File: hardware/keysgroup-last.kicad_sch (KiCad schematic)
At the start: 19 parts, among them SW65 SC4823S6-TR, SW66 SC4823S6-TR, SW67 SC4823S6-TR, SW68 SC4823S6-TR, SW69 SC4823S6-TR, SW70 SC4823S6-TR, SW71 SC4823S6-TR, SW72 SC4823S6-TR, SW73 SC4823S6-TR, SW74 SC4823S6-TR, SW75 SC4823S6-TR, SW76 SC4823S6-TR, SW77 SC4823S6-TR, SW78 SC4823S6-TR, T5 XL4067TS

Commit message: :construction: some chip layout
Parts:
- C29: symbol components:0402,100nF -> KeysDock:0402,100nF
- C30: symbol components:0402,4.7uF -> KeysDock:0402,4.7uF
- C31: symbol components:0402,10uF -> KeysDock:0402,10uF
- T5: symbol components:XL4067TS -> KeysDock:XL4067TS
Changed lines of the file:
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@@
 	)
 	(symbol
-		(lib_id "components:0402,10uF")
+		(lib_id "KeysDock:0402,10uF")
 		(at 247.65 129.54 0)
 		(unit 1)
@@
 	)
 	(symbol
-		(lib_id "components:0402,100nF")
+		(lib_id "KeysDock:0402,100nF")
 		(at 237.49 129.54 0)
 		(unit 1)
@@
 	)
 	(symbol
-		(lib_id "components:0402,4.7uF")
+		(lib_id "KeysDock:0402,4.7uF")
 		(at 242.57 129.54 0)
 		(unit 1)
@@
 	)
 	(symbol
-		(lib_id "components:XL4067TS")
+		(lib_id "KeysDock:XL4067TS")
 		(at 217.17 113.03 270)
 		(unit 1)

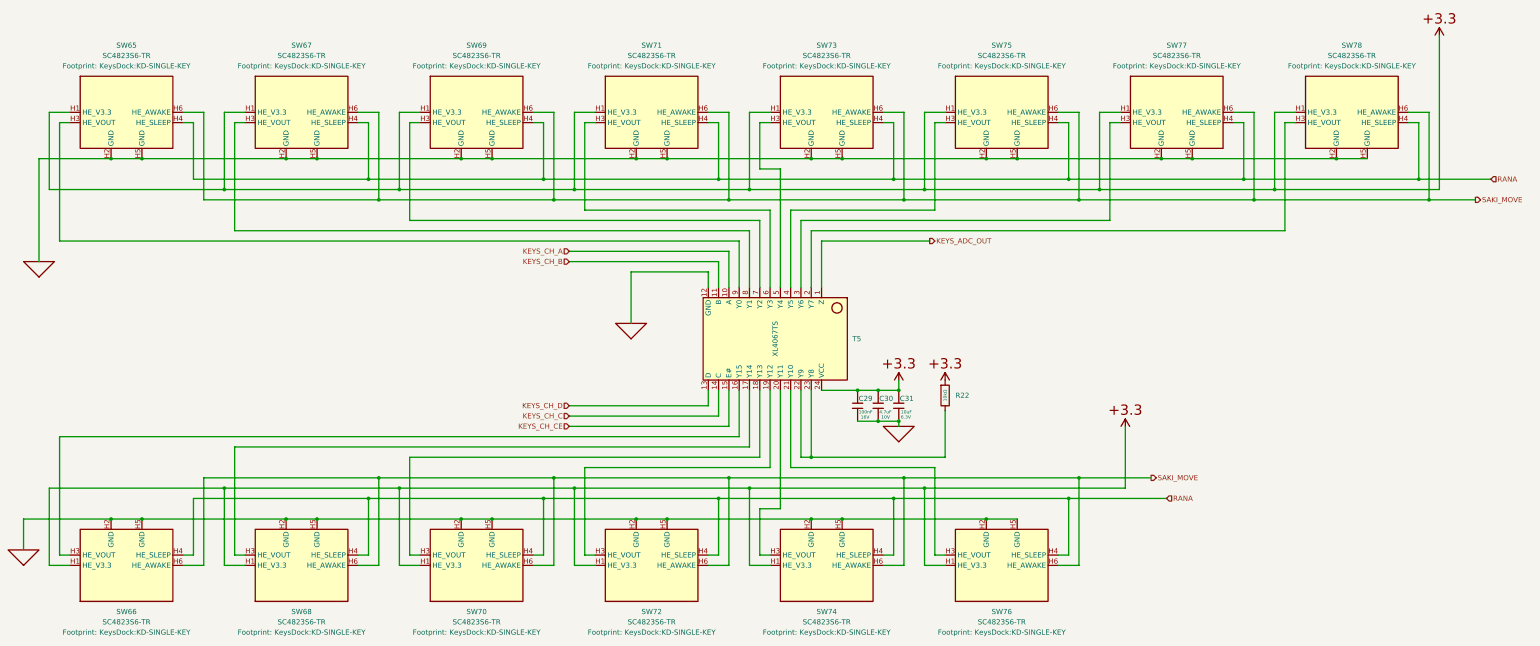
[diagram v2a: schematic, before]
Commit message: :sparkles: use net tie to construct GNDs
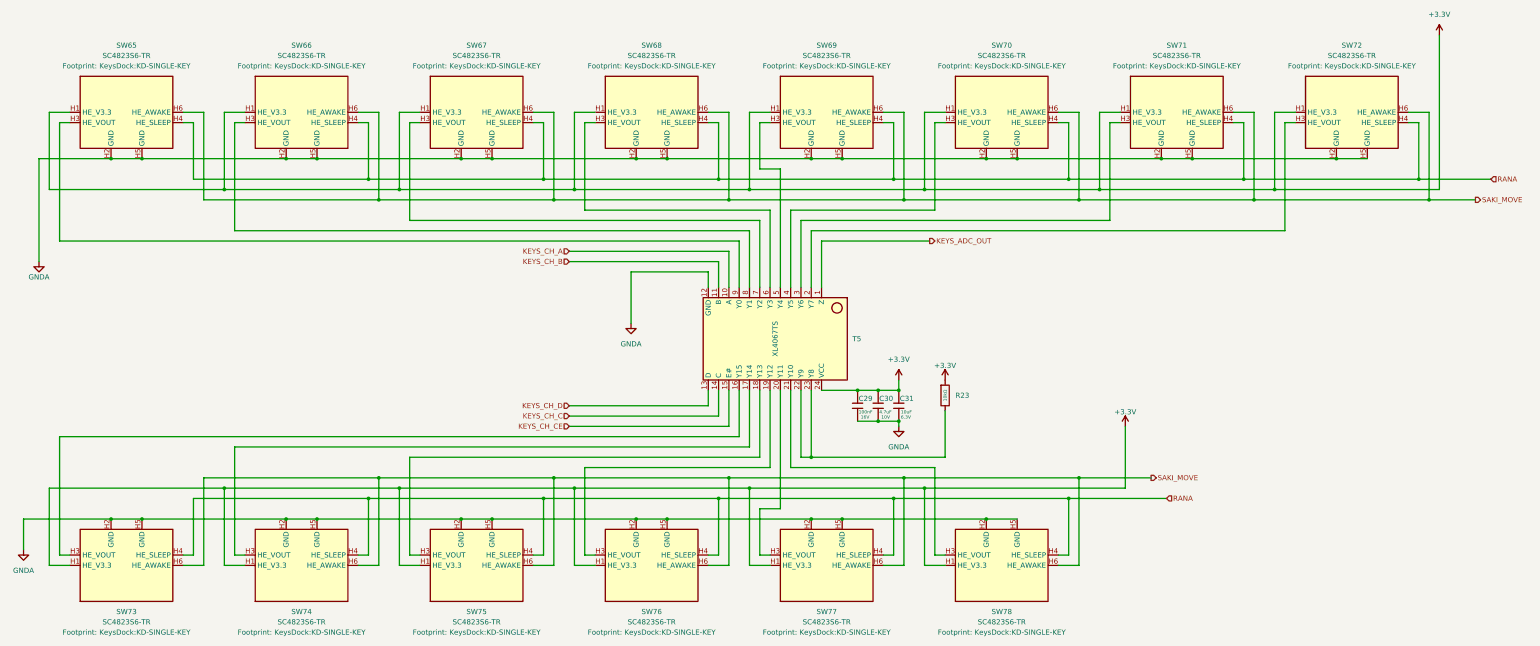
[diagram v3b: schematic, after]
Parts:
- renumbered R22 to R23, SW67 to SW66, SW69 to SW67, SW71 to SW68, SW73 to SW69, SW75 to SW70, SW77 to SW71, SW78 to SW72, SW66 to SW73, SW68 to SW74, SW70 to SW75, SW72 to SW76, SW74 to SW77, SW76 to SW78
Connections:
- net P,+3.3 renamed +3.3V
- net P,GND renamed GNDA
